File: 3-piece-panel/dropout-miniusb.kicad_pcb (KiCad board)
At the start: 2 copper layers, 228.6 x 94.4 mm, 51 parts, among them SW1 Rotary_Encoder_Switch, SW2 SW_Push, U1 ProMicro

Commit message: adding copper plated mounting holes
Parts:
- removed the mouse-bite-2mm-slot at (213.5, 69.7)
- removed the mouse-bite-2mm-slot at (213.5, 126.9)
- removed the mouse-bite-2mm-slot at (136.8, 126.2)
- removed the mouse-bite-2mm-slot at (136.8, 69.0)
- added H10: MountingHole, MountingHole:MountingHole_2.2mm_M2_Pad, F.Cu at (117.5, 69.3)
- added H11: MountingHole, MountingHole:MountingHole_2.2mm_M2_Pad, F.Cu at (270.9, 69.1)
- added H12: MountingHole, MountingHole:MountingHole_2.2mm_M2_Pad, F.Cu at (226.7, 69.1)
- added H13: MountingHole, MountingHole:MountingHole_2.2mm_M2_Pad, F.Cu at (232.8, 120.2)
- added H14: MountingHole, MountingHole:MountingHole_2.2mm_M2_Pad, F.Cu at (264.9, 126.2)
- added H15: MountingHole, MountingHole:MountingHole_2.2mm_M2_Pad, F.Cu at (251.9, 97.7)
- added H6: MountingHole, MountingHole:MountingHole_2.2mm_M2_Pad, F.Cu at (73.3, 69.3)
- added H7: MountingHole, MountingHole:MountingHole_2.2mm_M2_Pad, F.Cu at (79.4, 120.5)
- added H8: MountingHole, MountingHole:MountingHole_2.2mm_M2_Pad, F.Cu at (98.5, 97.9)
- added H9: MountingHole, MountingHole:MountingHole_2.2mm_M2_Pad, F.Cu at (111.5, 126.5)
- added mouse-bite-2mm-slot: VAL**, Panelization:mouse-bite-2mm-slot, F.Cu at (136.8, 69.0)
- added mouse-bite-2mm-slot: VAL**, Panelization:mouse-bite-2mm-slot, F.Cu at (136.8, 126.2)
- added mouse-bite-2mm-slot: VAL**, Panelization:mouse-bite-2mm-slot, F.Cu at (213.5, 69.8)
- added mouse-bite-2mm-slot: VAL**, Panelization:mouse-bite-2mm-slot, F.Cu at (213.5, 127.0)
- moved H5 0.08 mm to (150.0, 69.1)
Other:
- outline, holes or cut-outs redrawn
- net class JLCPCB added: clearance 0.127, trace_width 0.127, via_dia 0.8, via_drill 0.4
- rule trace_min: 0.2 -> 0.127
- board text added: "This side up"

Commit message: rev 0.4
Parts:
- removed the mouse-bite-2mm-slot at (136.8, 69.0)
- removed the mouse-bite-2mm-slot at (136.8, 126.2)
- removed the mouse-bite-2mm-slot at (213.5, 69.8)
- removed the mouse-bite-2mm-slot at (213.5, 127.0)
- added U2: ProMicro, promicro:ProMicro, F.Cu at (165.9, 66.0)
- added mouse-bite-2mm-slot: VAL**, Panelization:mouse-bite-2mm-slot, F.Cu at (136.8, 69.0)
- added mouse-bite-2mm-slot: VAL**, Panelization:mouse-bite-2mm-slot, F.Cu at (136.8, 126.2)
- added mouse-bite-2mm-slot: VAL**, Panelization:mouse-bite-2mm-slot, F.Cu at (213.5, 69.7)
- added mouse-bite-2mm-slot: VAL**, Panelization:mouse-bite-2mm-slot, F.Cu at (213.5, 126.9)
- H10, H11, H12, H13, H14, H15, H6, H7, H8, H9: footprint MountingHole:MountingHole_2.2mm_M2_Pad -> MountingHole:MountingHole_2.2mm_M2
- U1: moved to F.Cu
- moved SW2 53.0 mm to (194.3, 77.5)
- moved J-ISP1 44.9 mm to (197.9, 106.6)
- moved D3 0.68 mm to (149.6, 101.7)
- moved D8 0.68 mm to (168.7, 101.7)
- moved D12 0.55 mm to (187.7, 101.7)
- moved D17 0.55 mm to (206.8, 101.7)
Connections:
- J-ISP1 pad 1: COL0 -> ROW2
- J-ISP1 pad 3: COL1 -> COL2
- J-ISP1 pad 4: ROW1 -> ROW3
- U1 pad 10: ROW2 -> COL0
- U1 pad 11: ROW3 -> ROW1
- U1 pad 12: ROW4 -> NUMLED
- U1 pad 13: NUMLED -> ROW4
- U1 pad 14: ROW1 -> ROW3
- U1 pad 15: COL0 -> ROW2
- U1 pad 16: COL1 -> COL2
- U1 pad 17: (no net) -> COL3
- U1 pad 18: (no net) -> ROT-B
- U1 pad 19: (no net) -> ROT-A
- U1 pad 20: (no net) -> ROW0
- U1 pad 5: ROW0 -> (no net)
- U1 pad 6: ROT-A -> (no net)
- U1 pad 7: ROT-B -> (no net)
- U1 pad 8: COL3 -> (no net)
- U1 pad 9: COL2 -> COL1
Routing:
- net VCC: track 59.6 -> 120.1 mm, vias 1 -> 5
- net RESET: track 68.8 -> 115.4 mm, vias 2 -> 4
- net COL2: track 90.7 -> 117.7 mm, vias 0 -> 1
- net ROW3: track 106.4 -> 133.4 mm
- net COL0: track 122.2 -> 104.7 mm, vias 2 -> 1
- net ROW1: track 108.5 -> 93.0 mm, vias 0 -> 1
- net ROT-B: track 32.4 -> 43.8 mm
- net ROT-A: track 32.9 -> 42.7 mm
- net ROW4: track 97.8 -> 107.0 mm
- net COL3: track 126.8 -> 135.9 mm
- net NUMLED: track 40.7 -> 49.5 mm
- net ROW2: track 103.7 -> 112.4 mm
- net Net-(D6-Pad2): track 13.6 -> 16.7 mm
- net ROW0: track 72.4 -> 74.4 mm, vias 2 -> 3
- net Net-(D8-Pad2): track 8.37 -> 7.69 mm
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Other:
- board text added: "dropout by enochau rev0.4"
- board text removed: "This side up"
- board text removed: "dropout by enochau rev0.3"

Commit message: labels for orientation of pro-micro
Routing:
- net GND: track 0.00 -> 4.31 mm, vias 0 -> 1
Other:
- board text added: "RAW"
- board text added: "TX0"

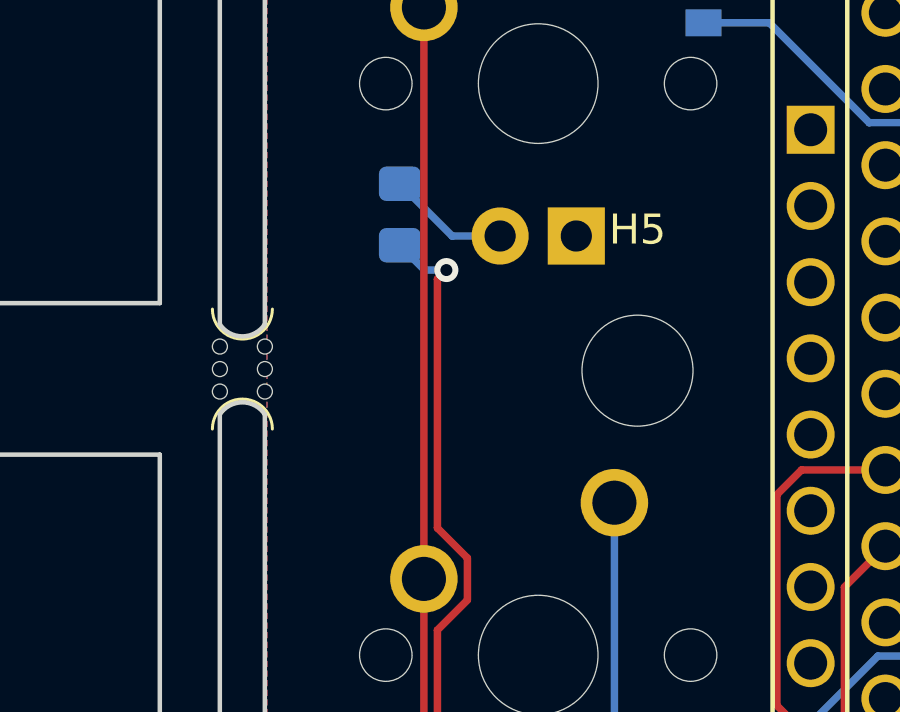
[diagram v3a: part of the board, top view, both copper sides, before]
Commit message: qmk backlight numlock
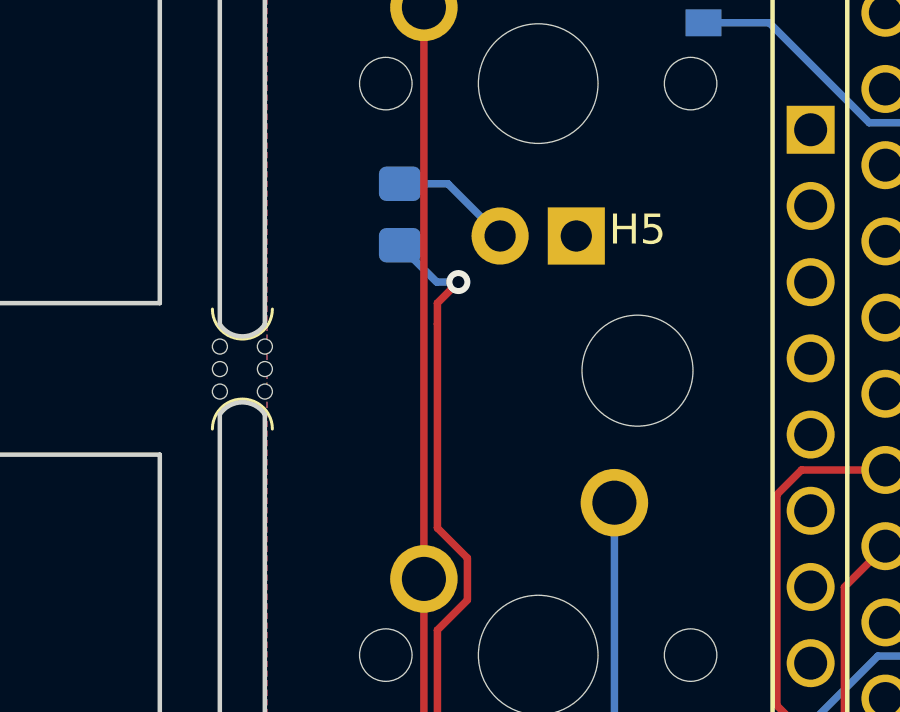
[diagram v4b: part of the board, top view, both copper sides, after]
